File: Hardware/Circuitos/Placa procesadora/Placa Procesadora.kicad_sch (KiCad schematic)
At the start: 6 parts, among them J1 Conn_01x02

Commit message: Placa procesadora - Componentes amplificación
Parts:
- added C6, C7: 10uF, Capacitor_THT:C_Radial_D5.0mm_H11.0mm_P2.00mm, symbol Device:C
- added R3, R7, R8: 1K, Resistor_THT:R_Axial_DIN0204_L3.6mm_D1.6mm_P7.62mm_Horizontal, symbol Device:R
- added R4, R9: 2.2K, Resistor_THT:R_Axial_DIN0204_L3.6mm_D1.6mm_P7.62mm_Horizontal, symbol Device:R
- added U1: LM358, symbol Amplifier_Operational:LM358

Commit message: Placa procesadora - Conexión amplificación
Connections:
- net 5V: now also U1.8 (V+)
- net Earth: now also C6.2, C7.2, U1.4 (V-)
- net at C6.1: now also R3.2
- net at R4.1: now also R3.1, U1.2 (-)
- net at R4.2: now also R7.1, U1.1
- net at U1.5 (+): now also R7.2
- net at U1.6 (-): now also R8.1, R9.1
- net at U1.7: now also R9.2
- net at U1.3 (+): now also C3.2
- net at C7.1: now also R8.2
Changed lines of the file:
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@@
+	)
+	(junction
+		(at 135.89 76.2)
+		(diameter 0)
+		(color 0 0 0 0)
 	)
 	(junction
@@
 		(color 0 0 0 0)
 	)
+	(junction
+		(at 144.78 90.17)
+		(diameter 0)
+		(color 0 0 0 0)
+	)
+	(junction
+		(at 109.22 87.63)
+		(diameter 0)
+		(color 0 0 0 0)
+	)
+	(wire
+		(pts
+			(xy 109.22 97.79) (xy 109.22 101.6)
+		)
+		(stroke
+			(width 0)
+			(type default)
+		)
+	)
 	(wire
 		(pts
@@
 	(wire
 		(pts
+			(xy 132.08 76.2) (xy 135.89 76.2)
+		)
+		(stroke
+			(width 0)
+			(type default)
+		)
+	)
+	(wire
+		(pts
+			(xy 91.44 73.66) (xy 116.84 73.66)
+		)
+		(stroke
+			(width 0)
+			(type default)
+		)
+	)
+	(wire
+		(pts
+			(xy 171.45 90.17) (xy 171.45 78.74)
+		)
+		(stroke
+			(width 0)
+			(type default)
+		)
+	)
+	(wire
+		(pts
 			(xy 77.47 86.36) (xy 77.47 88.9)
 		)
@@
 	(wire
 		(pts
+			(xy 144.78 90.17) (xy 144.78 92.71)
+		)
+		(stroke
+			(width 0)
+			(type default)
+		)
+	)
+	(wire
+		(pts
+			(xy 109.22 87.63) (xy 109.22 90.17)
+		)
+		(stroke
+			(width 0)
+			(type default)
+		)
+	)
+	(wire
+		(pts
+			(xy 109.22 109.22) (xy 109.22 113.03)
+		)
+		(stroke
+			(width 0)
+			(type default)
+		)
+	)
+	(wire
+		(pts
+			(xy 171.45 90.17) (xy 166.37 90.17)
+		)
+		(stroke
+			(width 0)
+			(type default)
+		)
+	)
+	(wire
+		(pts
+			(xy 135.89 87.63) (xy 135.89 76.2)
+		)
+		(stroke
+			(width 0)
+			(type default)
+		)
+	)
+	(wire
+		(pts
+			(xy 135.89 87.63) (xy 127 87.63)
+		)
+		(stroke
+			(width 0)
+			(type default)
+		)
+	)
+	(wire
+		(pts
+			(xy 148.59 76.2) (xy 152.4 76.2)
+		)
+		(stroke
+			(width 0)
+			(type default)
+		)
+	)
+	(wire
+		(pts
 			(xy 49.53 71.12) (xy 46.99 71.12)
 		)
@@
 	(wire
 		(pts
+			(xy 116.84 78.74) (xy 109.22 78.74)
+		)
+		(stroke
+			(width 0)
+			(type default)
+		)
+	)
+	(wire
+		(pts
 			(xy 73.66 73.66) (xy 77.47 73.66)
 		)
@@
 	(wire
 		(pts
+			(xy 153.67 59.69) (xy 149.86 59.69)
+		)
+		(stroke
+			(width 0)
+			(type default)
+		)
+	)
+	(wire
+		(pts
 			(xy 62.23 86.36) (xy 62.23 88.9)
 		)
@@
 	(wire
 		(pts
+			(xy 144.78 111.76) (xy 144.78 116.84)
+		)
+		(stroke
+			(width 0)
+			(type default)
+		)
+	)
+	(wire
+		(pts
 			(xy 62.23 73.66) (xy 62.23 78.74)
 		)
 		(stroke
+			(width 0)
+			(type default)
+		)
+	)
+	(wire
+		(pts
+			(xy 144.78 100.33) (xy 144.78 104.14)
+		)
+		(stroke
+			(width 0)
+			(type default)
+		)
+	)
+	(wire
+		(pts
+			(xy 144.78 81.28) (xy 144.78 90.17)
+		)
+		(stroke
+			(width 0)
+			(type default)
+		)
+	)
+	(wire
+		(pts
+			(xy 109.22 87.63) (xy 119.38 87.63)
+		)
+		(stroke
+			(width 0)
+			(type default)
+		)
+	)
+	(wire
+		(pts
+			(xy 152.4 81.28) (xy 144.78 81.28)
+		)
+		(stroke
+			(width 0)
+			(type default)
+		)
+	)
+	(wire
+		(pts
+			(xy 109.22 78.74) (xy 109.22 87.63)
+		)
+		(stroke
+			(width 0)
+			(type default)
+		)
+	)
+	(wire
+		(pts
+			(xy 167.64 78.74) (xy 171.45 78.74)
+		)
+		(stroke
+			(width 0)
+			(type default)
+		)
+	)
+	(wire
+		(pts
+			(xy 130.81 59.69) (xy 134.62 59.69)
+		)
+		(stroke
+			(width 0)
+			(type default)
+		)
+	)
+	(wire
+		(pts
+			(xy 135.89 76.2) (xy 140.97 76.2)
+		)
+		(stroke
+			(width 0)
+			(type default)
+		)
+	)
+	(wire
+		(pts
+			(xy 144.78 90.17) (xy 158.75 90.17)
+		)
+		(stroke

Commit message: Placa procesadora - Componentes adaptación ESP32
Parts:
- added C8, C9: 100nF, Capacitor_THT:C_Radial_D5.0mm_H11.0mm_P2.00mm, symbol Device:C
- added D5: BAT-85, Diode_THT:D_DO-35_SOD27_P7.62mm_Horizontal, symbol Device:D_Schottky
- added J2: Conn_01x02, Connector_Molex:Molex_KK-254_AE-6410-02A_1x02_P2.54mm_Vertical, symbol Connector_Generic:Conn_01x02
- added R10: 1M, Resistor_THT:R_Axial_DIN0204_L3.6mm_D1.6mm_P7.62mm_Horizontal, symbol Device:R
- added R11: 100k, Resistor_THT:R_Axial_DIN0204_L3.6mm_D1.6mm_P7.62mm_Horizontal, symbol Device:R

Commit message: Placa procesadora - Conexion adaptación
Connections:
- net Earth: now also C9.2, J2.2 (Pin_2), R10.2, R11.2
- net at D5.1 (K): now also C9.1, J2.1 (Pin_1), R10.1
- net at D5.2 (A): now also C8.2, R11.1
- net at R9.2, U1.7: now also C8.1
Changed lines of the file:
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@@
+	)
+	(junction
+		(at 171.45 78.74)
+		(diameter 0)
+		(color 0 0 0 0)
 	)
 	(junction
@@
 	)
 	(junction
+		(at 215.9 78.74)
+		(diameter 0)
+		(color 0 0 0 0)
+	)
+	(junction
 		(at 144.78 90.17)
 		(diameter 0)
@@
 	)
 	(junction
+		(at 204.47 78.74)
+		(diameter 0)
+		(color 0 0 0 0)
+	)
+	(junction
 		(at 109.22 87.63)
 		(diameter 0)
 		(color 0 0 0 0)
 	)
+	(junction
+		(at 187.325 78.74)
+		(diameter 0)
+		(color 0 0 0 0)
+	)
 	(wire
 		(pts
@@
 	(wire
 		(pts
+			(xy 171.45 78.74) (xy 176.53 78.74)
+		)
+		(stroke
+			(width 0)
+			(type default)
+		)
+	)
+	(wire
+		(pts
 			(xy 62.23 73.66) (xy 66.04 73.66)
 		)
@@
 	(wire
 		(pts
+			(xy 187.325 78.74) (xy 192.405 78.74)
+		)
+		(stroke
+			(width 0)
+			(type default)
+		)
+	)
+	(wire
+		(pts
 			(xy 49.53 68.58) (xy 49.53 71.12)
 		)
@@
 	(wire
 		(pts
+			(xy 224.79 81.28) (xy 224.79 96.52)
+		)
+		(stroke
+			(width 0)
+			(type default)
+		)
+	)
+	(wire
+		(pts
 			(xy 171.45 90.17) (xy 171.45 78.74)
 		)
@@
 	(wire
 		(pts
+			(xy 204.47 92.71) (xy 204.47 96.52)
+		)
+		(stroke
+			(width 0)
+			(type default)
+		)
+	)
+	(wire
+		(pts
 			(xy 144.78 90.17) (xy 144.78 92.71)
 		)
@@
 	(wire
 		(pts
+			(xy 204.47 78.74) (xy 204.47 85.09)
+		)
+		(stroke
+			(width 0)
+			(type default)
+		)
+	)
+	(wire
+		(pts
 			(xy 109.22 87.63) (xy 109.22 90.17)
 		)
@@
 	(wire
 		(pts
+			(xy 215.9 92.71) (xy 215.9 96.52)
+		)
+		(stroke
+			(width 0)
+			(type default)
+		)
+	)
+	(wire
+		(pts
 			(xy 109.22 109.22) (xy 109.22 113.03)
 		)
@@
 	(wire
 		(pts
+			(xy 187.325 92.075) (xy 187.325 96.52)
+		)
+		(stroke
+			(width 0)
+			(type default)
+		)
+	)
+	(wire
+		(pts
+			(xy 215.9 78.74) (xy 224.79 78.74)
+		)
+		(stroke
+			(width 0)
+			(type default)
+		)
+	)
+	(wire
+		(pts
 			(xy 77.47 73.66) (xy 83.82 73.66)
 		)
@@
 	(wire
 		(pts
+			(xy 200.025 78.74) (xy 204.47 78.74)
+		)
+		(stroke
+			(width 0)
+			(type default)
+		)
+	)
+	(wire
+		(pts
 			(xy 116.84 78.74) (xy 109.22 78.74)
 		)
@@
 	(wire
 		(pts
+			(xy 184.15 78.74) (xy 187.325 78.74)
+		)
+		(stroke
+			(width 0)
+			(type default)
+		)
+	)
+	(wire
+		(pts
 			(xy 62.23 86.36) (xy 62.23 88.9)
 		)
@@
 	(wire
 		(pts
+			(xy 215.9 85.09) (xy 215.9 78.74)
+		)
+		(stroke
+			(width 0)
+			(type default)
+		)
+	)
+	(wire
+		(pts
 			(xy 144.78 81.28) (xy 144.78 90.17)
 		)
@@
 	(wire
 		(pts
+			(xy 187.325 78.74) (xy 187.325 84.455)
+		)
+		(stroke
+			(width 0)
+			(type default)
+		)
+	)
+	(wire
+		(pts
 			(xy 46.99 73.66) (xy 50.8 73.66)
 		)
@@
 		)
 		(stroke
+			(width 0)
+			(type default)
+		)
+	)
+	(wire
+		(pts
+			(xy 215.9 78.74) (xy 204.47 78.74)
+		)
+		(stroke

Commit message: Placa procesadora - Componentes generador VBIAS
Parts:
- added C4: 10uF, Capacitor_THT:C_Radial_D5.0mm_H11.0mm_P2.00mm, symbol Device:C
- added C5: 100nF, Capacitor_THT:C_Radial_D5.0mm_H11.0mm_P2.00mm, symbol Device:C
- added J7: Conn_01x02, Connector_Molex:Molex_KK-254_AE-6410-02A_1x02_P2.54mm_Vertical, symbol Connector_Generic:Conn_01x02
- added R13: 100K, Resistor_THT:R_Axial_DIN0204_L3.6mm_D1.6mm_P7.62mm_Horizontal, symbol Device:R
- added R5, R6: 10K, Resistor_THT:R_Axial_DIN0204_L3.6mm_D1.6mm_P7.62mm_Horizontal, symbol Device:R

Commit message: Placa procesadora - Conexión generador VBIAS
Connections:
- net 5V: now also J7.1 (Pin_1), R5.1
- net Earth: now also C4.2, C5.2, J7.2 (Pin_2), R6.1
- net at R6.2: now also C4.1, C5.1, R13.1, R5.2
- net at C3.2, U1.3 (+): now also R13.2
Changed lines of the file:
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@@
+	)
+	(junction
+		(at 55.88 39.37)
+		(diameter 0)
+		(color 0 0 0 0)
+	)
+	(junction
+		(at 68.58 39.37)
+		(diameter 0)
+		(color 0 0 0 0)
+	)
+	(junction
+		(at 81.28 39.37)
+		(diameter 0)
+		(color 0 0 0 0)
 	)
 	(junction
@@
 	)
 	(junction
+		(at 55.88 27.94)
+		(diameter 0)
+		(color 0 0 0 0)
+	)
+	(junction
+		(at 106.68 73.66)
+		(diameter 0)
+		(color 0 0 0 0)
+	)
+	(junction
 		(at 144.78 90.17)
 		(diameter 0)
@@
 	(wire
 		(pts
+			(xy 81.28 39.37) (xy 106.68 39.37)
+		)
+		(stroke
+			(width 0)
+			(type default)
+		)
+	)
+	(wire
+		(pts
+			(xy 81.28 43.18) (xy 81.28 39.37)
+		)
+		(stroke
+			(width 0)
+			(type default)
+		)
+	)
+	(wire
+		(pts
 			(xy 171.45 78.74) (xy 176.53 78.74)
 		)
@@
 	(wire
 		(pts
+			(xy 55.88 49.53) (xy 55.88 54.61)
+		)
+		(stroke
+			(width 0)
+			(type default)
+		)
+	)
+	(wire
+		(pts
+			(xy 106.68 73.66) (xy 116.84 73.66)
+		)
+		(stroke
+			(width 0)
+			(type default)
+		)
+	)
+	(wire
+		(pts
+			(xy 106.68 60.96) (xy 106.68 73.66)
+		)
+		(stroke
+			(width 0)
+			(type default)
+		)
+	)
+	(wire
+		(pts
 			(xy 224.79 81.28) (xy 224.79 96.52)
 		)
@@
 	(wire
 		(pts
+			(xy 68.58 43.18) (xy 68.58 39.37)
+		)
+		(stroke
+			(width 0)
+			(type default)
+		)
+	)
+	(wire
+		(pts
 			(xy 171.45 90.17) (xy 171.45 78.74)
 		)
@@
 	(wire
 		(pts
+			(xy 55.88 27.94) (xy 55.88 29.21)
+		)
+		(stroke
+			(width 0)
+			(type default)
+		)
+	)
+	(wire
+		(pts
 			(xy 215.9 78.74) (xy 224.79 78.74)
 		)
@@
 	(wire
 		(pts
+			(xy 68.58 39.37) (xy 81.28 39.37)
+		)
+		(stroke
+			(width 0)
+			(type default)
+		)
+	)
+	(wire
+		(pts
 			(xy 58.42 73.66) (xy 62.23 73.66)
 		)
@@
 	(wire
 		(pts
+			(xy 81.28 50.8) (xy 81.28 54.61)
+		)
+		(stroke
+			(width 0)
+			(type default)
+		)
+	)
+	(wire
+		(pts
 			(xy 200.025 78.74) (xy 204.47 78.74)
 		)
@@
 	(wire
 		(pts
+			(xy 68.58 50.8) (xy 68.58 54.61)
+		)
+		(stroke
+			(width 0)
+			(type default)
+		)
+	)
+	(wire
+		(pts
 			(xy 73.66 73.66) (xy 77.47 73.66)
 		)
@@
 	(wire
 		(pts
+			(xy 106.68 39.37) (xy 106.68 53.34)
+		)
+		(stroke
+			(width 0)
+			(type default)
+		)
+	)
+	(wire
+		(pts
+			(xy 49.53 27.94) (xy 55.88 27.94)
+		)
+		(stroke
+			(width 0)
+			(type default)
+		)
+	)
+	(wire
+		(pts
 			(xy 184.15 78.74) (xy 187.325 78.74)
 		)
@@
 	(wire
 		(pts
+			(xy 55.88 39.37) (xy 68.58 39.37)
+		)
+		(stroke
+			(width 0)
+			(type default)
+		)
+	)
+	(wire
+		(pts
+			(xy 55.88 39.37) (xy 55.88 41.91)
+		)
+		(stroke
+			(width 0)
+			(type default)
+		)
+	)
+	(wire
+		(pts
 			(xy 62.23 86.36) (xy 62.23 88.9)
 		)
@@
 	(wire
 		(pts
-			(xy 91.44 73.66) (xy 116.84 73.66)
+			(xy 91.44 73.66) (xy 106.68 73.66)
 		)
 		(stroke
@@
 		)
 		(stroke
+			(width 0)
+			(type default)
+		)
+	)
+	(wire
+		(pts
+			(xy 58.42 27.94) (xy 64.77 27.94)
+		)
+		(stroke

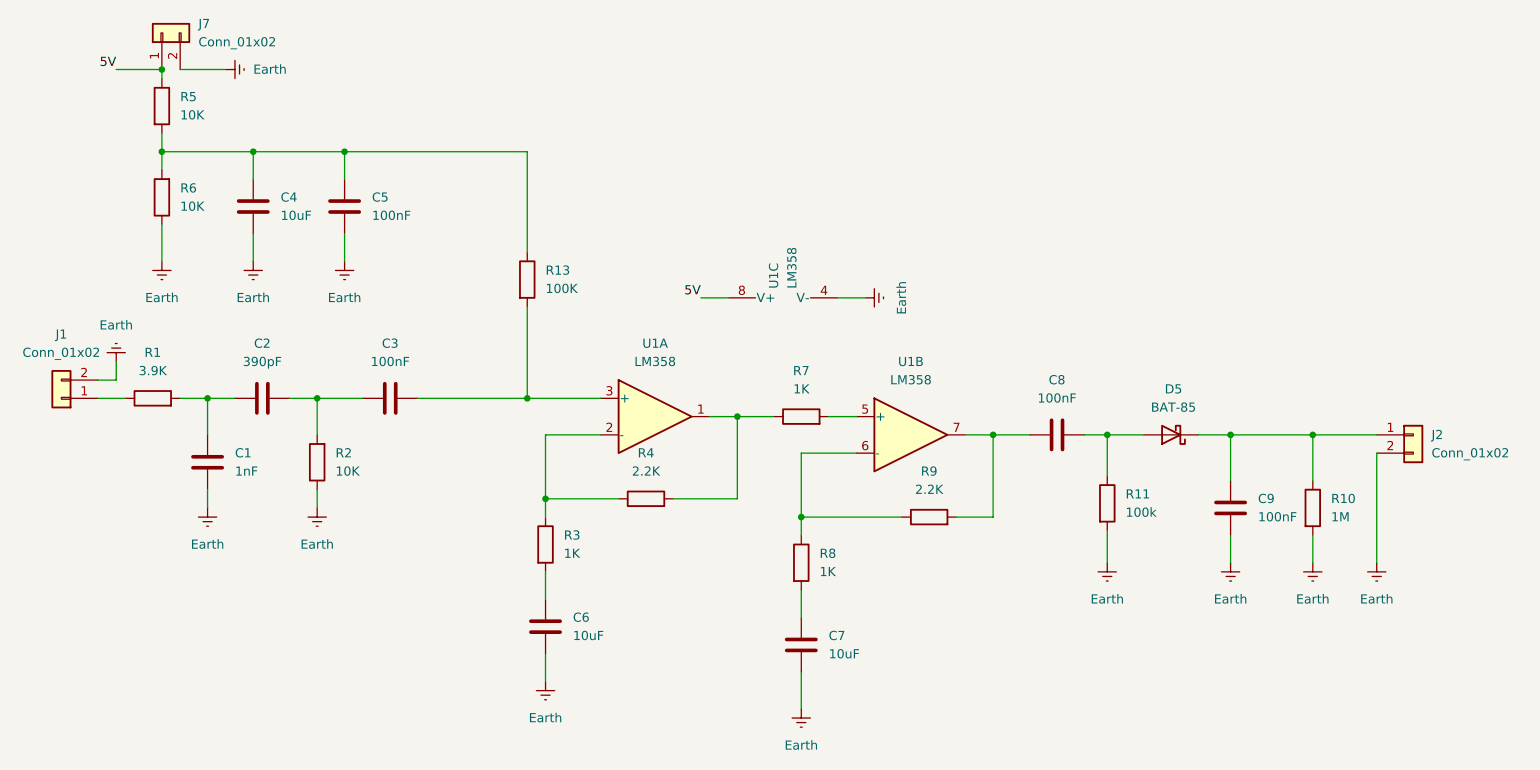
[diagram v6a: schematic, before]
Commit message: Placa procesadora - Colocación de filtro
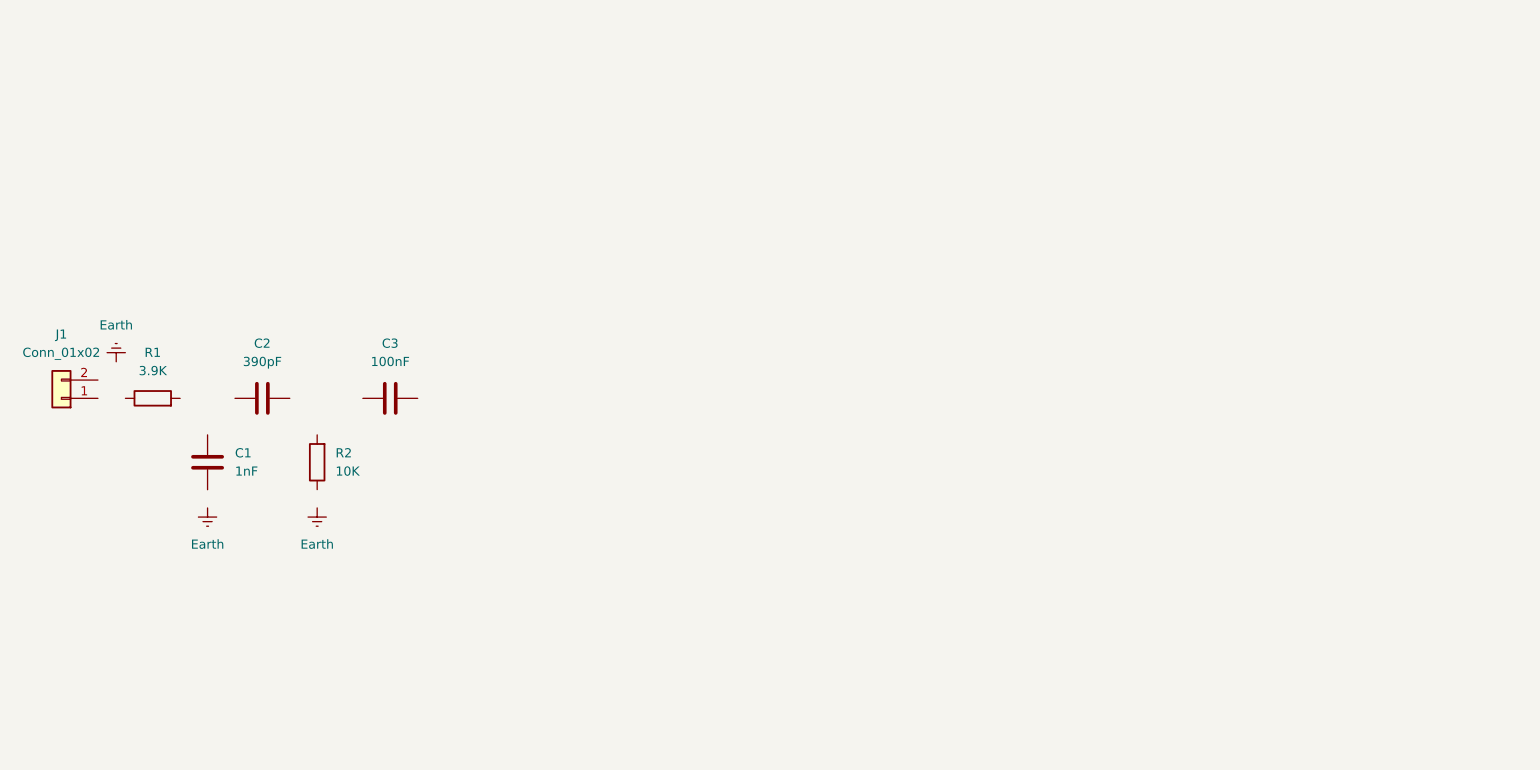
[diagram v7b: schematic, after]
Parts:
- removed C4, C6, C7: 10uF, Capacitor_THT:C_Radial_D5.0mm_H11.0mm_P2.00mm, symbol Device:C
- removed C5, C8, C9: 100nF, Capacitor_THT:C_Radial_D5.0mm_H11.0mm_P2.00mm, symbol Device:C
- removed D5: BAT-85, Diode_THT:D_DO-35_SOD27_P7.62mm_Horizontal, symbol Device:D_Schottky
- removed J2, J7: Conn_01x02, Connector_Molex:Molex_KK-254_AE-6410-02A_1x02_P2.54mm_Vertical, symbol Connector_Generic:Conn_01x02
- removed R10: 1M, Resistor_THT:R_Axial_DIN0204_L3.6mm_D1.6mm_P7.62mm_Horizontal, symbol Device:R
- removed R11: 100k, Resistor_THT:R_Axial_DIN0204_L3.6mm_D1.6mm_P7.62mm_Horizontal, symbol Device:R
- removed R13: 100K, Resistor_THT:R_Axial_DIN0204_L3.6mm_D1.6mm_P7.62mm_Horizontal, symbol Device:R
- removed R3, R7, R8: 1K, Resistor_THT:R_Axial_DIN0204_L3.6mm_D1.6mm_P7.62mm_Horizontal, symbol Device:R
- removed R4, R9: 2.2K, Resistor_THT:R_Axial_DIN0204_L3.6mm_D1.6mm_P7.62mm_Horizontal, symbol Device:R
- removed R5, R6: 10K, Resistor_THT:R_Axial_DIN0204_L3.6mm_D1.6mm_P7.62mm_Horizontal, symbol Device:R
- removed U1: LM358, symbol Amplifier_Operational:LM358
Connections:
- net Earth: no longer C1.2, J1.2 (Pin_2), R2.1
- net at R1.1: no longer J1.1 (Pin_1)
- now unconnected: C1.1, C2.1, C2.2, C3.1, R1.2, R2.2

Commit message: Placa procesadora - Conexión de filtros
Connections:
- net Earth: now also C1.2, J1.2 (Pin_2), R2.1
- net at C1.1: now also C2.1, R1.2
- net at C2.2: now also C3.1, R2.2
- net at R1.1: now also J1.1 (Pin_1)
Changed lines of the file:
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@@
 	(generator_version "10.0")
 	(paper "A4")
+	(junction
+		(at 77.47 73.66)
+		(diameter 0)
+		(color 0 0 0 0)
+	)
+	(junction
+		(at 62.23 73.66)
+		(diameter 0)
+		(color 0 0 0 0)
+	)
+	(wire
+		(pts
+			(xy 62.23 73.66) (xy 66.04 73.66)
+		)
+		(stroke
+			(width 0)
+			(type default)
+		)
+	)
+	(wire
+		(pts
+			(xy 49.53 68.58) (xy 49.53 71.12)
+		)
+		(stroke
+			(width 0)
+			(type default)
+		)
+	)
+	(wire
+		(pts
+			(xy 77.47 86.36) (xy 77.47 88.9)
+		)
+		(stroke
+			(width 0)
+			(type default)
+		)
+	)
+	(wire
+		(pts
+			(xy 49.53 71.12) (xy 46.99 71.12)
+		)
+		(stroke
+			(width 0)
+			(type default)
+		)
+	)
+	(wire
+		(pts
+			(xy 77.47 73.66) (xy 83.82 73.66)
+		)
+		(stroke
+			(width 0)
+			(type default)
+		)
+	)
+	(wire
+		(pts
+			(xy 58.42 73.66) (xy 62.23 73.66)
+		)
+		(stroke
+			(width 0)
+			(type default)
+		)
+	)
+	(wire
+		(pts
+			(xy 73.66 73.66) (xy 77.47 73.66)
+		)
+		(stroke
+			(width 0)
+			(type default)
+		)
+	)
+	(wire
+		(pts
+			(xy 62.23 86.36) (xy 62.23 88.9)
+		)
+		(stroke
+			(width 0)
+			(type default)
+		)
+	)
+	(wire
+		(pts
+			(xy 62.23 73.66) (xy 62.23 78.74)
+		)
+		(stroke
+			(width 0)
+			(type default)
+		)
+	)
+	(wire
+		(pts
+			(xy 46.99 73.66) (xy 50.8 73.66)
+		)
+		(stroke
+			(width 0)
+			(type default)
+		)
+	)
+	(wire
+		(pts
+			(xy 77.47 73.66) (xy 77.47 78.74)
+		)
+		(stroke
+			(width 0)
+			(type default)
+		)
+	)
 	(symbol
 		(lib_id "Device:C")
